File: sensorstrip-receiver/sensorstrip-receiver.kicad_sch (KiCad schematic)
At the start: 6 parts, among them J1 Conn_01x02_MountingPin, J2 Conn_01x02_MountingPin

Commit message: fix humongous oversight
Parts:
- renumbered D3 to D1, D1 to D3
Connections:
- net GND: no longer D2.1 (K), D3.1 (K)
- net LEDs renamed D3+
- net D3+: no longer D1.2 (A), D2.2 (A)
- new net D1+: D1.2 (A), D2.1 (K)
- new net D2+: D2.2 (A), D3.1 (K)
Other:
- moved on the sheet: D1, D2, D3
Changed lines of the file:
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@@
   (junction (at 117.348 86.868) (diameter 0) (color 0 0 0 0)
   )
-  (junction (at 63.754 83.058) (diameter 0) (color 0 0 0 0)
-  )
-  (junction (at 100.584 91.44) (diameter 0) (color 0 0 0 0)
-  )
-  (junction (at 63.754 91.44) (diameter 0) (color 0 0 0 0)
-  )
   (junction (at 120.65 86.868) (diameter 0) (color 0 0 0 0)
   )
   (junction (at 115.57 91.44) (diameter 0) (color 0 0 0 0)
   )
-  (wire (pts (xy 88.9 91.44) (xy 63.754 91.44))
-    (stroke (width 0) (type default) (color 0 0 0 0))
-  )
-  (wire (pts (xy 63.754 83.058) (xy 63.754 77.47))
-    (stroke (width 0) (type default) (color 0 0 0 0))
-  )
-  (wire (pts (xy 100.584 98.552) (xy 96.266 98.552))
+  (wire (pts (xy 78.232 91.44) (xy 75.184 91.44))
     (stroke (width 0) (type default) (color 0 0 0 0))
   )
@@
     (stroke (width 0) (type default) (color 0 0 0 0))
   )
-  (wire (pts (xy 63.754 91.44) (xy 63.754 98.552))
-    (stroke (width 0) (type default) (color 0 0 0 0))
-  )
   (wire (pts (xy 120.65 86.868) (xy 117.348 86.868))
     (stroke (width 0) (type default) (color 0 0 0 0))
@@
     (stroke (width 0) (type default) (color 0 0 0 0))
   )
-  (wire (pts (xy 101.346 91.44) (xy 100.584 91.44))
-    (stroke (width 0) (type default) (color 0 0 0 0))
-  )
-  (wire (pts (xy 88.646 98.552) (xy 63.754 98.552))
-    (stroke (width 0) (type default) (color 0 0 0 0))
-  )
-  (wire (pts (xy 63.754 83.058) (xy 63.754 91.44))
-    (stroke (width 0) (type default) (color 0 0 0 0))
-  )
-  (wire (pts (xy 100.584 83.058) (xy 96.52 83.058))
-    (stroke (width 0) (type default) (color 0 0 0 0))
-  )
-  (wire (pts (xy 100.584 91.44) (xy 100.584 83.058))
+  (wire (pts (xy 67.564 91.44) (xy 63.754 91.44))
+    (stroke (width 0) (type default) (color 0 0 0 0))
+  )
+  (wire (pts (xy 63.754 77.47) (xy 63.754 91.44))
+    (stroke (width 0) (type default) (color 0 0 0 0))
+  )
+  (wire (pts (xy 88.646 91.44) (xy 85.852 91.44))
     (stroke (width 0) (type default) (color 0 0 0 0))
   )
@@
     (stroke (width 0) (type default) (color 0 0 0 0))
   )
-  (wire (pts (xy 88.9 83.058) (xy 63.754 83.058))
-    (stroke (width 0) (type default) (color 0 0 0 0))
-  )
   (wire (pts (xy 115.57 86.868) (xy 115.57 88.9))
     (stroke (width 0) (type default) (color 0 0 0 0))
   )
-  (wire (pts (xy 100.584 91.44) (xy 100.584 98.552))
-    (stroke (width 0) (type default) (color 0 0 0 0))
-  )
-  (wire (pts (xy 100.584 91.44) (xy 96.52 91.44))
+  (wire (pts (xy 96.266 91.44) (xy 101.346 91.44))
     (stroke (width 0) (type default) (color 0 0 0 0))
   )
@@
     (effects (font (size 1.27 1.27)) (justify left bottom))
   )
-  (label "LEDs" (at 96.52 83.058 0)
+  (label "D2+" (at 86.106 91.44 0)
+    (effects (font (size 1.27 1.27)) (justify left bottom))
+  )
+  (label "D3+" (at 96.52 91.44 0)
+    (effects (font (size 1.27 1.27)) (justify left bottom))
+  )
+  (label "D1+" (at 75.184 91.44 0)
     (effects (font (size 1.27 1.27)) (justify left bottom))
   )
@@
     )
   )
-  (symbol (lib_id "Device:LED") (at 92.456 98.552 0) (unit 1)
-    (in_bom yes) (on_board yes)
-    (property "Reference" "D3" (id 0) (at 88.646 101.9718 0)
-      (effects (font (size 1.27 1.27)) (justify right))
-    )
-    (property "Value" "LED" (id 1) (at 88.646 104.5087 0)
-      (effects (font (size 1.27 1.27)) (justify right))
-    )
-    (property "Footprint" "sensorstrip:LED_THT-1.27mm-OrthogonalSMDAndTHT" (id 2) (at 92.456 98.552 0)
-      (effects (font (size 1.27 1.27)) hide)
-    )
-    (property "Datasheet" "~" (id 3) (at 92.456 98.552 0)
+  (symbol (lib_id "Device:LED") (at 71.374 91.44 0) (unit 1)
+    (in_bom yes) (on_board yes)
+    (property "Reference" "D1" (id 0) (at 67.564 94.8598 0)
+      (effects (font (size 1.27 1.27)) (justify right))
+    )
+    (property "Value" "LED" (id 1) (at 67.564 97.3967 0)
+      (effects (font (size 1.27 1.27)) (justify right))
+    )
+    (property "Footprint" "sensorstrip:LED_THT-1.27mm-OrthogonalSMDAndTHT" (id 2) (at 71.374 91.44 0)
+      (effects (font (size 1.27 1.27)) hide)
+    )
+    (property "Datasheet" "~" (id 3) (at 71.374 91.44 0)
       (effects (font (size 1.27 1.27)) hide)
     )
@@
     (pin "MP")
   )
-  (symbol (lib_id "Device:LED") (at 92.71 91.44 0) (unit 1)
-    (in_bom yes) (on_board yes)
-    (property "Reference" "D2" (id 0) (at 88.9 94.8598 0)
-      (effects (font (size 1.27 1.27)) (justify right))
-    )
-    (property "Value" "LED" (id 1) (at 88.9 97.3967 0)
-      (effects (font (size 1.27 1.27)) (justify right))
-    )
-    (property "Footprint" "sensorstrip:LED_THT-1.27mm-OrthogonalSMDAndTHT" (id 2) (at 92.71 91.44 0)
-      (effects (font (size 1.27 1.27)) hide)
-    )
-    (property "Datasheet" "~" (id 3) (at 92.71 91.44 0)
+  (symbol (lib_id "Device:LED") (at 82.042 91.44 0) (unit 1)
+    (in_bom yes) (on_board yes)
+    (property "Reference" "D2" (id 0) (at 78.232 94.8598 0)
+      (effects (font (size 1.27 1.27)) (justify right))
+    )
+    (property "Value" "LED" (id 1) (at 78.232 97.3967 0)
+      (effects (font (size 1.27 1.27)) (justify right))
+    )
+    (property "Footprint" "sensorstrip:LED_THT-1.27mm-OrthogonalSMDAndTHT" (id 2) (at 82.042 91.44 0)
+      (effects (font (size 1.27 1.27)) hide)
+    )
+    (property "Datasheet" "~" (id 3) (at 82.042 91.44 0)
       (effects (font (size 1.27 1.27)) hide)
     )
@@
     (pin "1")
   )
-  (symbol (lib_id "Device:LED") (at 92.71 83.058 0) (unit 1)
-    (in_bom yes) (on_board yes)
-    (property "Reference" "D1" (id 0) (at 89.408 87.4394 0)
-      (effects (font (size 1.27 1.27)) (justify right))
-    )
-    (property "Value" "LED" (id 1) (at 89.408 89.9794 0)
-      (effects (font (size 1.27 1.27)) (justify right))
-    )
-    (property "Footprint" "sensorstrip:LED_THT-1.27mm-OrthogonalSMDAndTHT" (id 2) (at 92.71 83.058 0)
-      (effects (font (size 1.27 1.27)) hide)
-    )
-    (property "Datasheet" "~" (id 3) (at 92.71 83.058 0)
+  (symbol (lib_id "Device:LED") (at 92.456 91.44 0) (unit 1)
+    (in_bom yes) (on_board yes)
+    (property "Reference" "D3" (id 0) (at 89.154 95.8214 0)
+      (effects (font (size 1.27 1.27)) (justify right))
+    )
+    (property "Value" "LED" (id 1) (at 89.154 98.3614 0)
+      (effects (font (size 1.27 1.27)) (justify right))
+    )
+    (property "Footprint" "sensorstrip:LED_THT-1.27mm-OrthogonalSMDAndTHT" (id 2) (at 92.456 91.44 0)
+      (effects (font (size 1.27 1.27)) hide)
+    )
+    (property "Datasheet" "~" (id 3) (at 92.456 91.44 0)
       (effects (font (size 1.27 1.27)) hide)
     )
@@
       (reference "#PWR0101") (unit 1) (value "GND") (footprint "")
     )
-    (path "/cb16ca99-563a-4e3e-999e-31e3640245a2"
+    (path "/0ddf7455-9149-4dbc-979b-f086dbd57a6e"
       (reference "D1") (unit 1) (value "LED") (footprint "sensorstrip:LED_THT-1.27mm-OrthogonalSMDAndTHT")
     )
@@
       (reference "D2") (unit 1) (value "LED") (footprint "sensorstrip:LED_THT-1.27mm-OrthogonalSMDAndTHT")
     )
-    (path "/0ddf7455-9149-4dbc-979b-f086dbd57a6e"
+    (path "/cb16ca99-563a-4e3e-999e-31e3640245a2"
       (reference "D3") (unit 1) (value "LED") (footprint "sensorstrip:LED_THT-1.27mm-OrthogonalSMDAndTHT")
     )

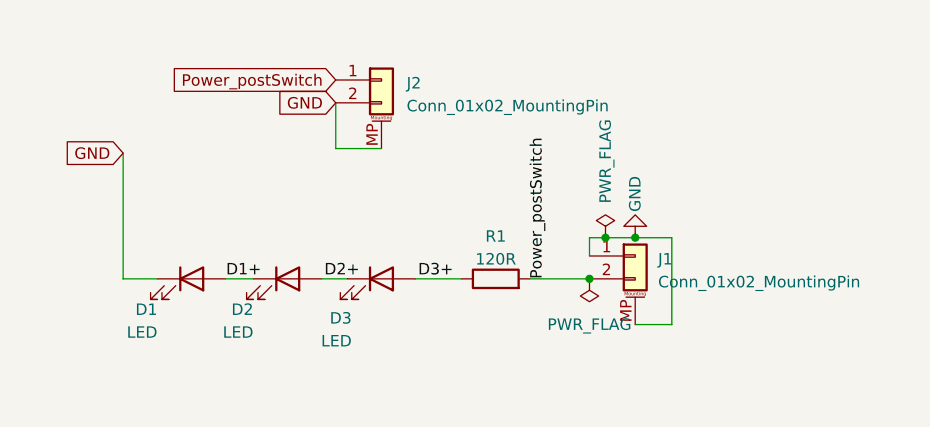
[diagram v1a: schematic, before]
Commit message: Cleanup in preparation for push
Update project files to KiCad 7 format
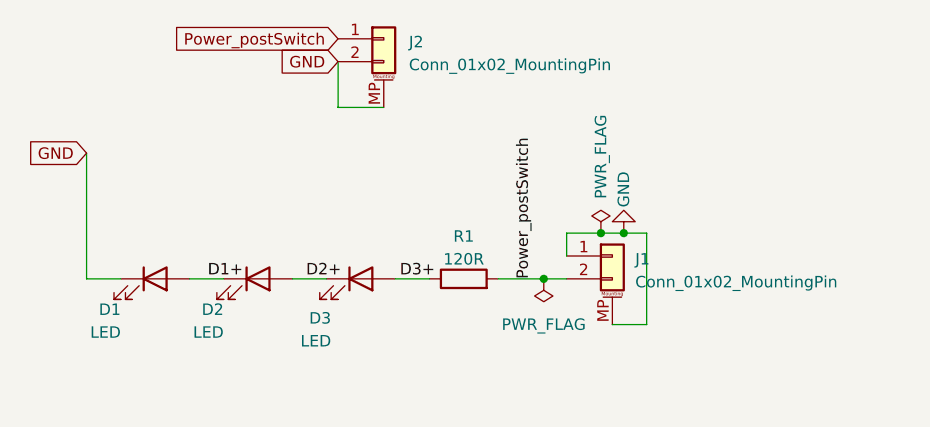
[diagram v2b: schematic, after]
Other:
- moved on the sheet: D1, D2, D3, J1, J2, R1

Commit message: Add 4IR+2IR switchable power board
Minor cleanup
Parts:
- J1, J2: footprint Connector_Molex:Molex_PicoBlade_53261-0271_1x02-1MP_P1.25mm_Horizontal -> sensorstrip:Molex_Picoblade_53261-0271-Hybrid
